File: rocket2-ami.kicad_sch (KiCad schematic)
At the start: 51 parts, among them J1 ARM Cortex Debug, J3 XT60 POWER, U1 STM32F105RCT6, U2 LD1086DT33TR, U4 USBLC6-2SC6, U5 ADXL383, Y1 8MHz

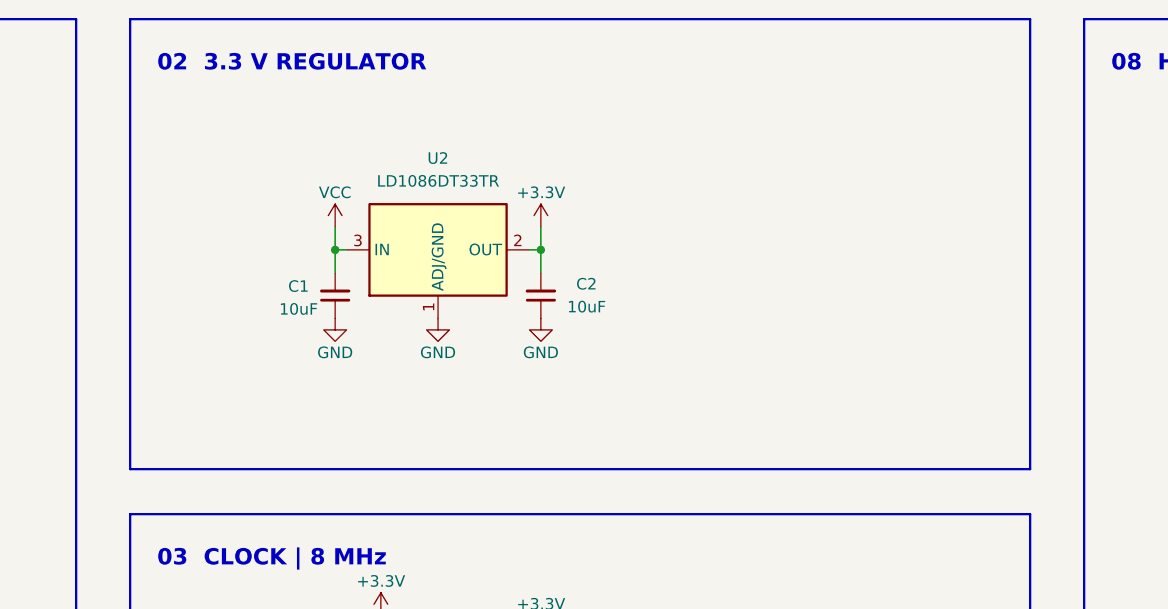
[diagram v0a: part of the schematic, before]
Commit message: Switched to buck convertor!
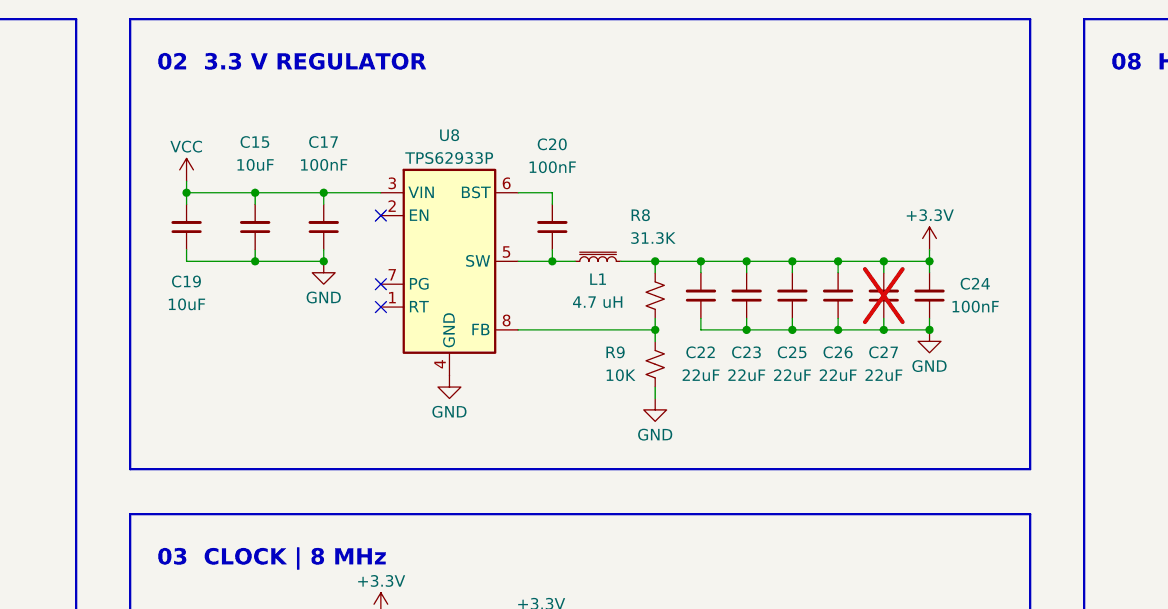
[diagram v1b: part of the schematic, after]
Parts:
- removed C1, C2: 10uF, Capacitor_SMD:C_0603_1608Metric, symbol Device:C_Small
- removed U2: LD1086DT33TR, Package_TO_SOT_SMD:TO-252-2, symbol Regulator_Linear:LD1086DT33TR
- added C15, C19: 10uF, Capacitor_SMD:C_0603_1608Metric, symbol Device:C_Small
- added C17, C20, C24: 100nF, Capacitor_SMD:C_0603_1608Metric, symbol Device:C_Small
- added C22, C23, C25, C26, C27: 22uF, Capacitor_SMD:C_0603_1608Metric, symbol Device:C_Small
- added L1: 4.7 uH, 0UCIRP-KiCAD-Lib:Inductor (4.7uH) IND_03-4R7-R_EAT, symbol Device:L_Iron_Small
- added R8: 31.3K, Resistor_SMD:R_0402_1005Metric, symbol Device:R_Small_US
- added R9: 10K, Resistor_SMD:R_0402_1005Metric, symbol Device:R_Small_US
- added U8: TPS62933P, Package_TO_SOT_SMD:SOT-583-8, symbol Regulator_Switching:TPS62933P
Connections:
- net +3.3V: now also C22.2, C23.2, C24.2, C25.2, C26.2, C27.2, L1.2, R8.1
- net GND: now also C15.1, C17.1, C19.1, C22.1, C23.1, C24.1, C25.1, C26.1, C27.1, R9.2, U8.4 (GND)
- net VCC: now also C15.2, C17.2, C19.2, U8.3 (VIN)
- new net: R8.2, R9.1, U8.8 (FB)
- new net: C20.1, L1.1, U8.5 (SW)
- new net: C20.2, U8.6 (BST)
- no-connect marks 33 -> 36

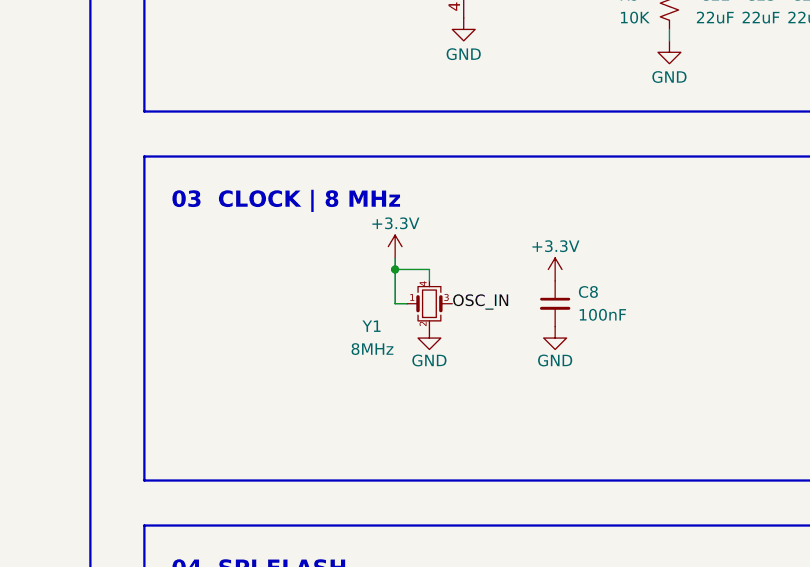
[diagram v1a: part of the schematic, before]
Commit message: Upgraded to 16 mhz clock (same as our other boards)
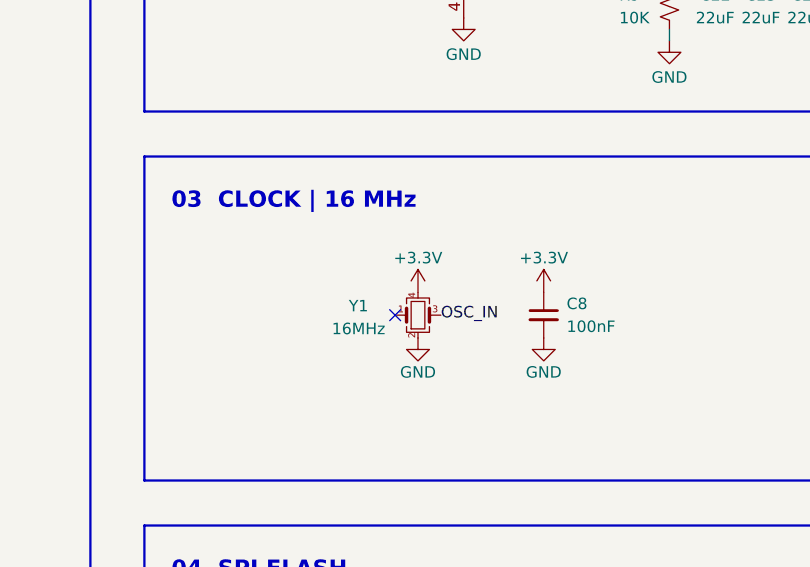
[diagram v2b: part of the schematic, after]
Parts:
- Y1: value 8MHz -> 16MHz; footprint Crystal:Crystal_SMD_2520-4Pin_2.5x2.0mm -> Crystal:Crystal_SMD_2016-4Pin_2.0x1.6mm; Part # ASDMB-8-000MHZ-XY-T -> ECS-1633-160-BN-TR
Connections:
- net +3.3V: no longer Y1.1
- no-connect marks 36 -> 37
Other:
- note added: "03 CLOCK | 16 MHz"
- note removed: "03 CLOCK | 8 MHz"
- moved on the sheet: C8, Y1
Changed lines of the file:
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@@
 		)
 	)
-	(text "03  CLOCK | 8 MHz"
+	(text "03  CLOCK | 16 MHz"
 		(exclude_from_sim no)
 		(at 125 75 0)
@@
 	)
 	(junction
-		(at 149.86 82.55)
-		(diameter 0)
-		(color 0 0 0 0)
-	)
-	(junction
 		(at 200.66 49.53)
 		(diameter 0)
@@
 	)
 	(no_connect
+		(at 149.86 87.63)
+	)
+	(no_connect
 		(at 87.63 115.57)
 	)
@@
 	(wire
 		(pts
-			(xy 149.86 86.36) (xy 149.86 82.55)
-		)
-		(stroke
-			(width 0)
-			(type default)
-		)
-	)
-	(wire
-		(pts
 			(xy 130.81 248.92) (xy 130.81 251.46)
 		)
@@
 	(wire
 		(pts
-			(xy 149.86 82.55) (xy 149.86 81.28)
-		)
-		(stroke
-			(width 0)
-			(type default)
-		)
-	)
-	(wire
-		(pts
 			(xy 58.42 255.27) (xy 58.42 262.89)
 		)
@@
 	(wire
 		(pts
-			(xy 153.67 82.55) (xy 149.86 82.55)
-		)
-		(stroke
-			(width 0)
-			(type default)
-		)
-	)
-	(wire
-		(pts
 			(xy 275.59 82.55) (xy 275.59 69.85)
 		)
@@
 	(wire
 		(pts
-			(xy 151.13 86.36) (xy 149.86 86.36)
-		)
-		(stroke
-			(width 0)
-			(type default)
-		)
-	)
-	(wire
-		(pts
 			(xy 149.86 34.29) (xy 143.51 34.29)
 		)
@@
 	(wire
 		(pts
-			(xy 153.67 83.82) (xy 153.67 82.55)
-		)
-		(stroke
-			(width 0)
-			(type default)
-		)
-	)
-	(wire
-		(pts
 			(xy 168.91 41.91) (xy 171.45 41.91)
 		)
@@
 	)
 	(label "OSC_IN"
-		(at 156.21 86.36 0)
+		(at 154.94 87.63 0)
 		(effects
 			(font
@@
 	(symbol
 		(lib_id "power:GND")
-		(at 167.64 88.9 0)
+		(at 166.37 90.17 0)
 		(unit 1)
 		(exclude_from_sim no)
@@
 		(dnp no)
 		(property "Reference" "#PWR019"
-			(at 167.64 95.25 0)
+			(at 166.37 96.52 0)
 			(effects
 				(font
@@
 		)
 		(property "Value" "GND"
-			(at 167.64 92.71 0)
+			(at 166.37 93.98 0)
 			(effects
 				(font
@@
 		)
 		(property "Footprint" ""
-			(at 167.64 88.9 0)
+			(at 166.37 90.17 0)
 			(effects
 				(font
@@
 		)
 		(property "Datasheet" ""
-			(at 167.64 88.9 0)
+			(at 166.37 90.17 0)
 			(effects
 				(font
@@
 		)
 		(property "Description" ""
-			(at 167.64 88.9 0)
+			(at 166.37 90.17 0)
 			(effects
 				(font
@@
 	(symbol
 		(lib_id "power:GND")
-		(at 153.67 88.9 0)
+		(at 152.4 90.17 0)
 		(unit 1)
 		(exclude_from_sim no)
@@
 		(dnp no)
 		(property "Reference" "#PWR026"
-			(at 153.67 95.25 0)
+			(at 152.4 96.52 0)
 			(effects
 				(font
@@
 		)
 		(property "Value" "GND"
-			(at 153.67 92.71 0)
+			(at 152.4 93.98 0)
 			(effects
 				(font
@@
 		)
 		(property "Footprint" ""
-			(at 153.67 88.9 0)
+			(at 152.4 90.17 0)
 			(effects
 				(font
@@
 		)
 		(property "Datasheet" ""
-			(at 153.67 88.9 0)
+			(at 152.4 90.17 0)
 			(effects
 				(font
@@
 		)
 		(property "Description" ""
-			(at 153.67 88.9 0)
+			(at 152.4 90.17 0)
 			(effects
 				(font
@@
 	(symbol
 		(lib_id "Device:Crystal_GND24_Small")
-		(at 153.67 86.36 0)
+		(at 152.4 87.63 0)
 		(unit 1)
 		(exclude_from_sim no)
@@
 		(dnp no)
 		(property "Reference" "Y1"
-			(at 147.32 88.9 0)
+			(at 145.796 86.614 0)
 			(effects
 				(font
@@
 			)
 		)
-		(property "Value" "8MHz"
-			(at 147.32 91.44 0)
+		(property "Value" "16MHz"
+			(at 145.796 89.154 0)
 			(effects
 				(font
@@
 			)
 		)
-		(property "Footprint" "Crystal:Crystal_SMD_2520-4Pin_2.5x2.0mm"
-			(at 153.67 86.36 0)
+		(property "Footprint" "Crystal:Crystal_SMD_2016-4Pin_2.0x1.6mm"
+			(at 152.4 87.63 0)
 			(effects
 				(font
@@
 			)
 		)
-		(property "Datasheet" "https://www.digikey.com/en/products/detail/abracon-llc/ASDMB-8-000MHZ-XY-T/2623866"
-			(at 153.67 86.36 0)
+		(property "Datasheet" "https://www.digikey.com/en/products/detail/ecs-inc/ECS-1633-160-BN-TR/8593603"
+			(at 152.4 87.63 0)
 			(effects
 				(font
@@
 		)
 		(property "Description" ""
-			(at 153.67 86.36 0)
+			(at 152.4 87.63 0)
 			(effects
 				(font
@@
 		)
 		(property "Manufacturer" "ECS"
-			(at 153.67 86.36 0)
+			(at 152.4 87.63 0)
 			(effects
 				(font
@@
 			)
 		)
-		(property "Part #" "ASDMB-8-000MHZ-XY-T"
-			(at 153.67 86.36 0)
+		(property "Part #" "ECS-1633-160-BN-TR"
+			(at 152.4 87.63 0)
 			(effects
 				(font
@@
 		)
 		(property "Field7" ""
-			(at 153.67 86.36 0)
+			(at 152.4 87.63 0)
 			(effects
 				(font
@@
 	(symbol
 		(lib_id "power:+3.3V")
-		(at 149.86 81.28 0)
+		(at 152.4 85.09 0)
 		(unit 1)
 		(exclude_from_sim no)
@@
 		(dnp no)
 		(property "Reference" "#PWR025"
-			(at 149.86 85.09 0)
+			(at 152.4 88.9 0)
 			(effects
 				(font
@@
 		)
 		(property "Value" "+3.3V"
-			(at 149.86 77.47 0)
+			(at 152.4 81.28 0)
 			(effects
 				(font
@@
 		)
 		(property "Footprint" ""
-			(at 149.86 81.28 0)
+			(at 152.4 85.09 0)
 			(effects
 				(font
@@
 		)
 		(property "Datasheet" ""
-			(at 149.86 81.28 0)
+			(at 152.4 85.09 0)
 			(effects
 				(font
@@
 		)
 		(property "Description" ""
-			(at 149.86 81.28 0)
+			(at 152.4 85.09 0)
 			(effects
 				(font
@@
 	(symbol
 		(lib_id "Device:C_Small")
-		(at 167.64 86.36 0)
+		(at 166.37 87.63 0)
 		(unit 1)
 		(exclude_from_sim no)
@@
 		(fields_autoplaced yes)
 		(property "Reference" "C8"
-			(at 170.18 85.0963 0)
+			(at 168.91 86.3663 0)
 			(effects
 				(font
@@
 		)
 		(property "Value" "100nF"
-			(at 170.18 87.6363 0)
+			(at 168.91 88.9063 0)
 			(effects
 				(font
@@
 		)
 		(property "Footprint" "Capacitor_SMD:C_0603_1608Metric"
-			(at 167.64 86.36 0)
+			(at 166.37 87.63 0)
 			(effects
 				(font
@@
 		)
 		(property "Datasheet" ""
-			(at 167.64 86.36 0)
+			(at 166.37 87.63 0)
 			(effects
 				(font
@@
 		)
 		(property "Description" ""
-			(at 167.64 86.36 0)
+			(at 166.37 87.63 0)
 			(effects
 				(font
@@
 		)
 		(property "Manufacturer" "Generic"
-			(at 167.64 86.36 0)
+			(at 166.37 87.63 0)
 			(effects
 				(font
@@
 		)
 		(property "Part #" "Generic 0603 6.3V 100nF X7R MLCC"
-			(at 167.64 86.36 0)
+			(at 166.37 87.63 0)
 			(effects
 				(font
@@
 	(symbol
 		(lib_id "power:+3.3V")
-		(at 167.64 83.82 0)
+		(at 166.37 85.09 0)
 		(unit 1)
 		(exclude_from_sim no)
@@
 		(dnp no)
 		(property "Reference" "#PWR020"
-			(at 167.64 87.63 0)
+			(at 166.37 88.9 0)
 			(effects
 				(font
@@
 		)
 		(property "Value" "+3.3V"
-			(at 167.64 80.01 0)
+			(at 166.37 81.28 0)
 			(effects
 				(font
@@
 		)
 		(property "Footprint" ""
-			(at 167.64 83.82 0)
+			(at 166.37 85.09 0)
 			(effects
 				(font
@@
 		)
 		(property "Datasheet" ""
-			(at 167.64 83.82 0)
+			(at 166.37 85.09 0)
 			(effects
 				(font
@@
 		)
 		(property "Description" ""
-			(at 167.64 83.82 0)
+			(at 166.37 85.09 0)
 			(effects
 				(font

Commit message: Updated schematic & layout to remove all ERC & DRC errors & all ERC warnings
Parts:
- J2: symbol UCIRP-KiCAD-Lib:USB-C -> UCIRP-KiCAD-Lib:Connector USB-C
- Y1: symbol Device:Crystal_GND24_Small -> UCIRP-KiCAD-Lib:Crystal_GND24_Small
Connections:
- net IMU_INT2: no longer names the net of U6.1 (INT2)
- net IMU_INT4: no longer names the net of U6.13 (INT4)
- no-connect marks 37 -> 51

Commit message: Added LED and UART
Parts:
- added C1: 4.7uF, Capacitor_SMD:C_0603_1608Metric, symbol Device:C_Small
- added C2: 100nF, Capacitor_SMD:C_0603_1608Metric, symbol Device:C_Small
- added D1: LED_ARGB, 0UCIRP-KiCAD-Lib:LED RGB (0606) APTF1616LSEEZGKQBKC, symbol Device:LED_ARGB
- added J4: Conn_01x04_Pin, Connector_PinHeader_2.54mm:PinHeader_1x04_P2.54mm_Vertical, symbol Connector:Conn_01x04_Pin
- added R10: 10K, Resistor_SMD:R_0603_1608Metric, symbol Device:R_Small_US
- added R11, R12: 325, Resistor_SMD:R_0402_1005Metric, symbol Device:R_Small_US
- added R17: 750, Resistor_SMD:R_0402_1005Metric, symbol Device:R_Small_US
- R8: Part # Generic RES SMD 10K OHM 1% 1/16W 0402 -> (none)
- U30: symbol UCIRP-KiCAD-Lib:TC_ADC MAX31855JASA+ -> UCIRP-KiCAD-Lib:TC_ADC_(K_Type)_MAX31855KASA+; Part # MAX31855JASA+ -> MAX31855KASA+
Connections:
- net +3.3V: now also C1.1, D1.1 (A), J4.1 (Pin_1), R10.2
- net GND: now also C1.2, C2.2, J4.4 (Pin_4)
- net ~{RST}: now also C2.1, R10.1
- net LED_B: now reaches U1.27 (PB1)
- net LED_B: now also R12.2
- net LED_G: now reaches U1.29 (PB10)
- net LED_G: now also R11.2
- net LED_R: now reaches U1.30 (PB11)
- net LED_R: now also R17.2
- net LoRA_TX: now reaches U1.51 (PC10)
- net LoRA_TX: now also J4.2 (Pin_2)
- net LoRA_RX: now reaches U1.52 (PC11)
- net LoRA_RX: now also J4.3 (Pin_3)
- new net: D1.2 (RK), R17.1
- new net: D1.4 (BK), R12.1
- new net: D1.3 (GK), R11.1
- no-connect marks 51 -> 46
